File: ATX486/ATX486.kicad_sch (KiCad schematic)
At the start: 1 part

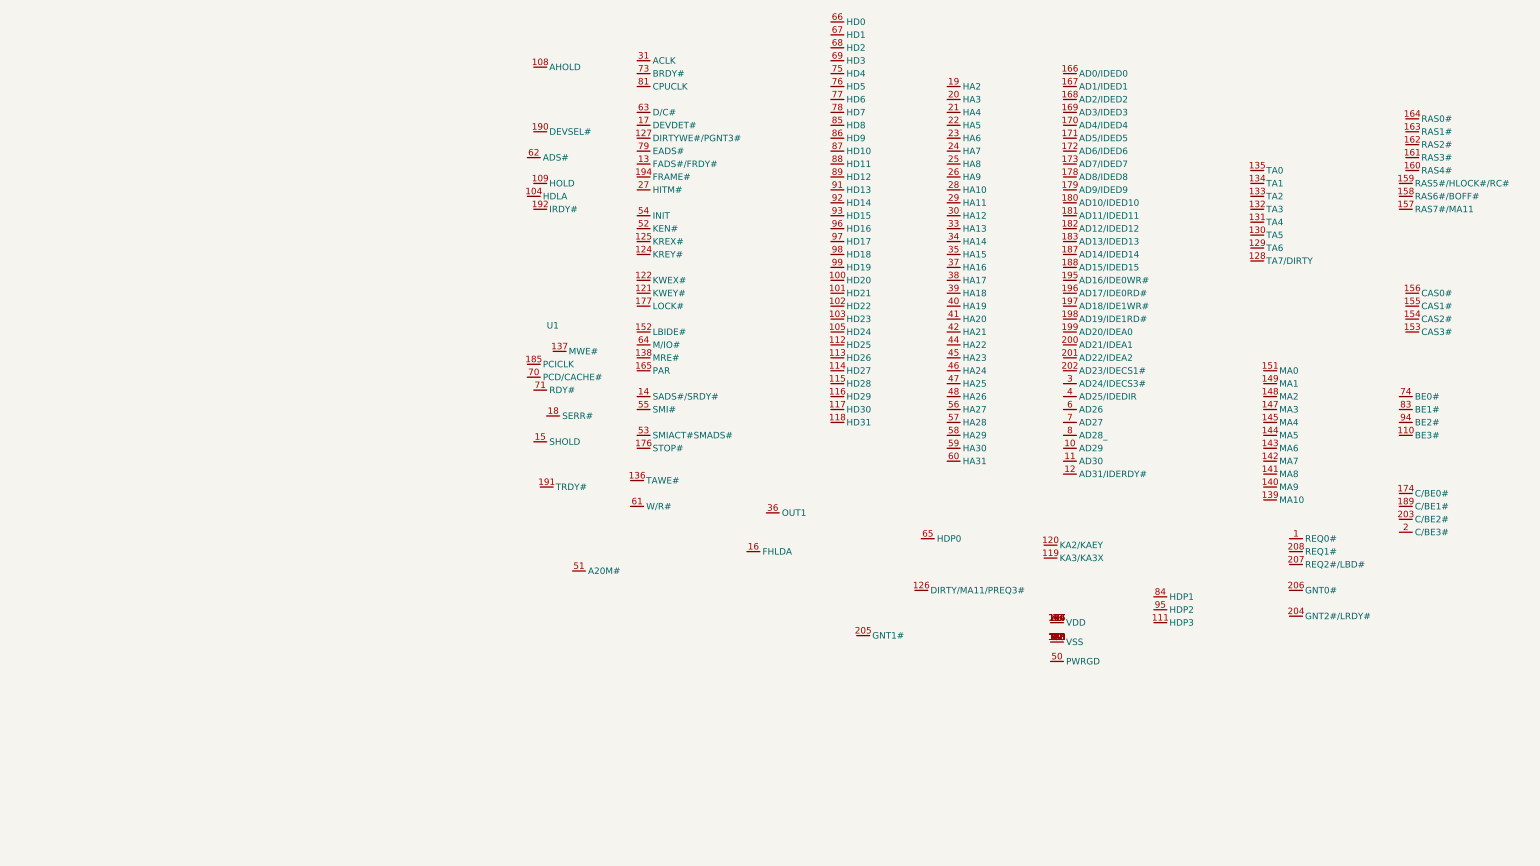
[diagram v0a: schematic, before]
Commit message: Added initial southbridge info
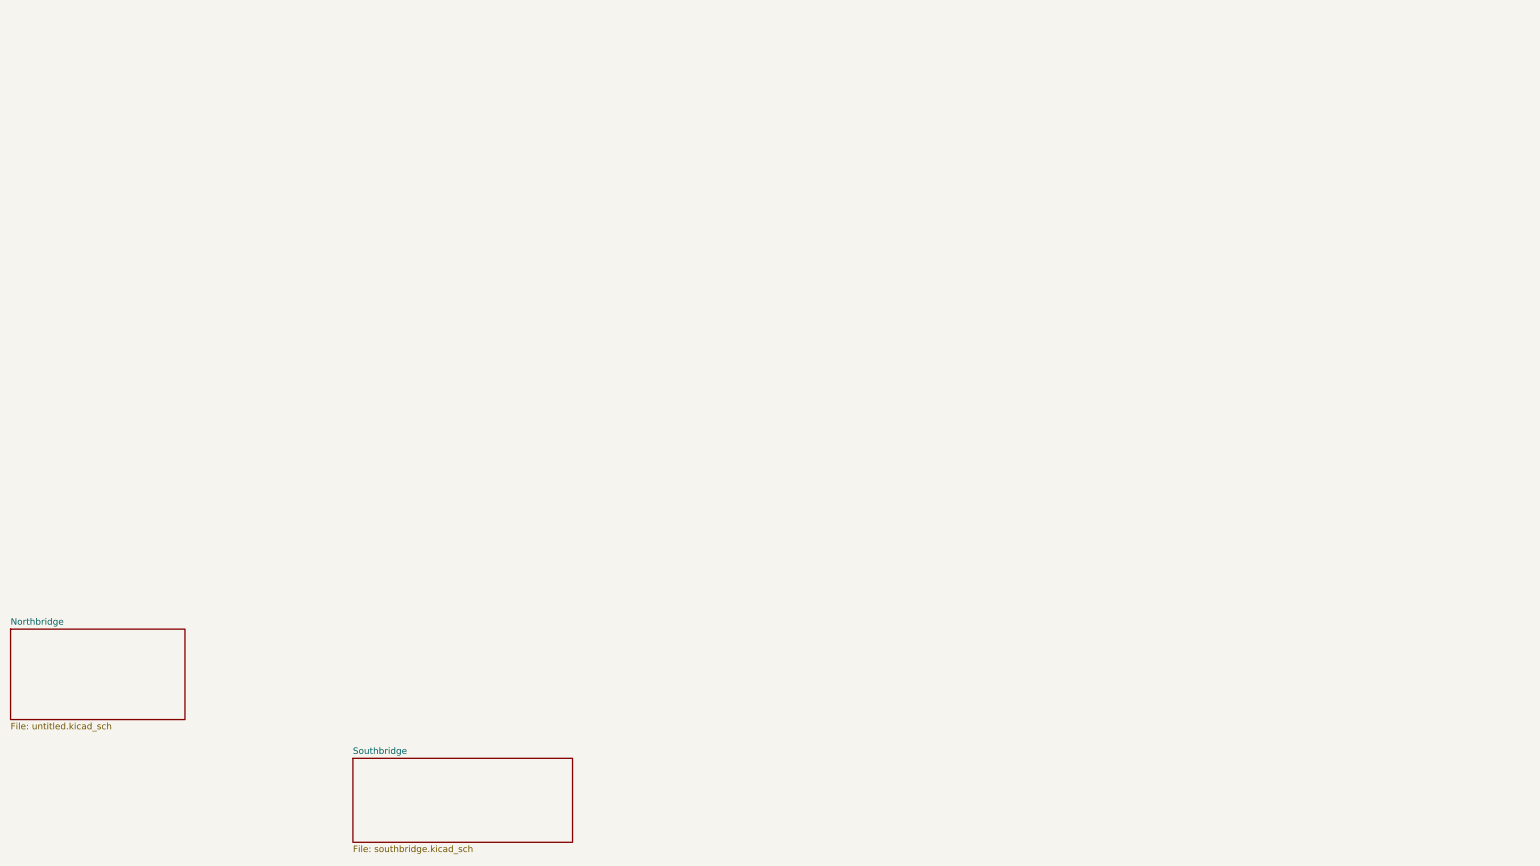
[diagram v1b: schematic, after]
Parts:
- removed U1: ~, Library:85c496, symbol New_Library:85C496
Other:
- added sheet Northbridge (untitled.kicad_sch)
- added sheet Southbridge (southbridge.kicad_sch)
